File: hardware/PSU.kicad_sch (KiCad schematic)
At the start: 19 parts, among them J1 UJ20-C-H-G-SMT-2A-P16-TR, U2 REF35330QDBVR, U4 LM27762, U5 NCP1117-3.3_SOT223

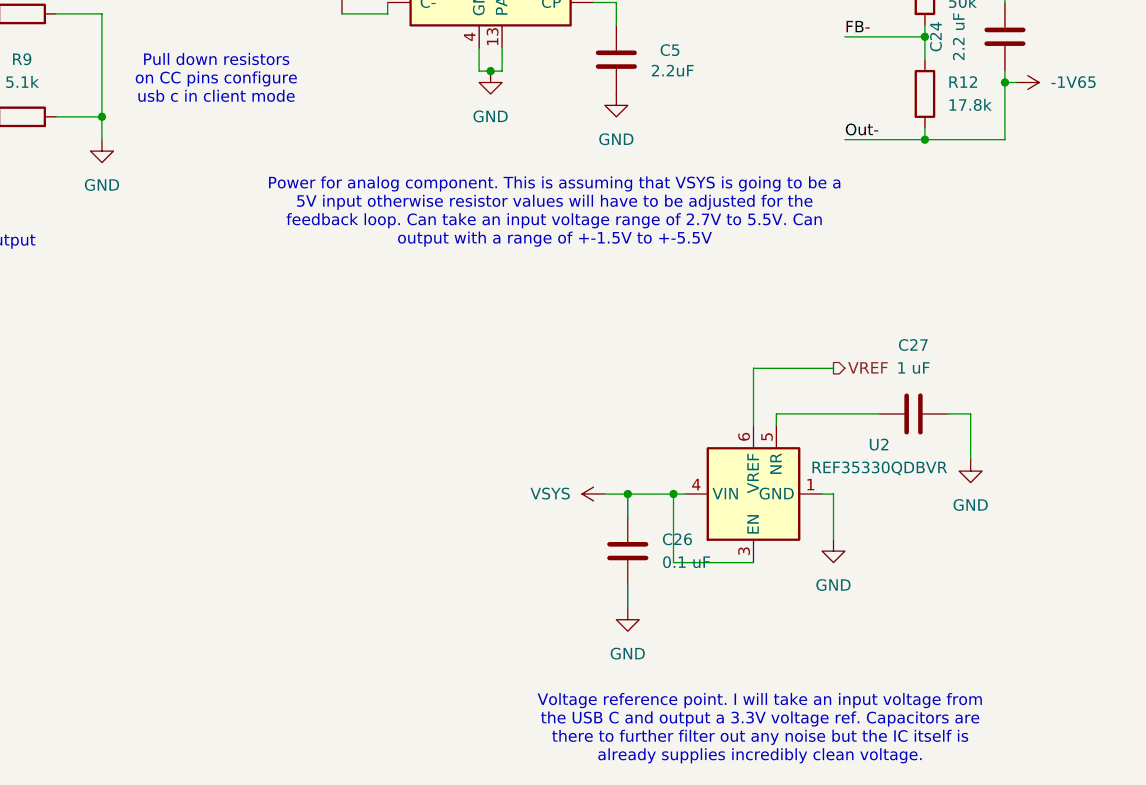
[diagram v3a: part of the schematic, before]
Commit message: "Updated PSU, Updated spreadsheets
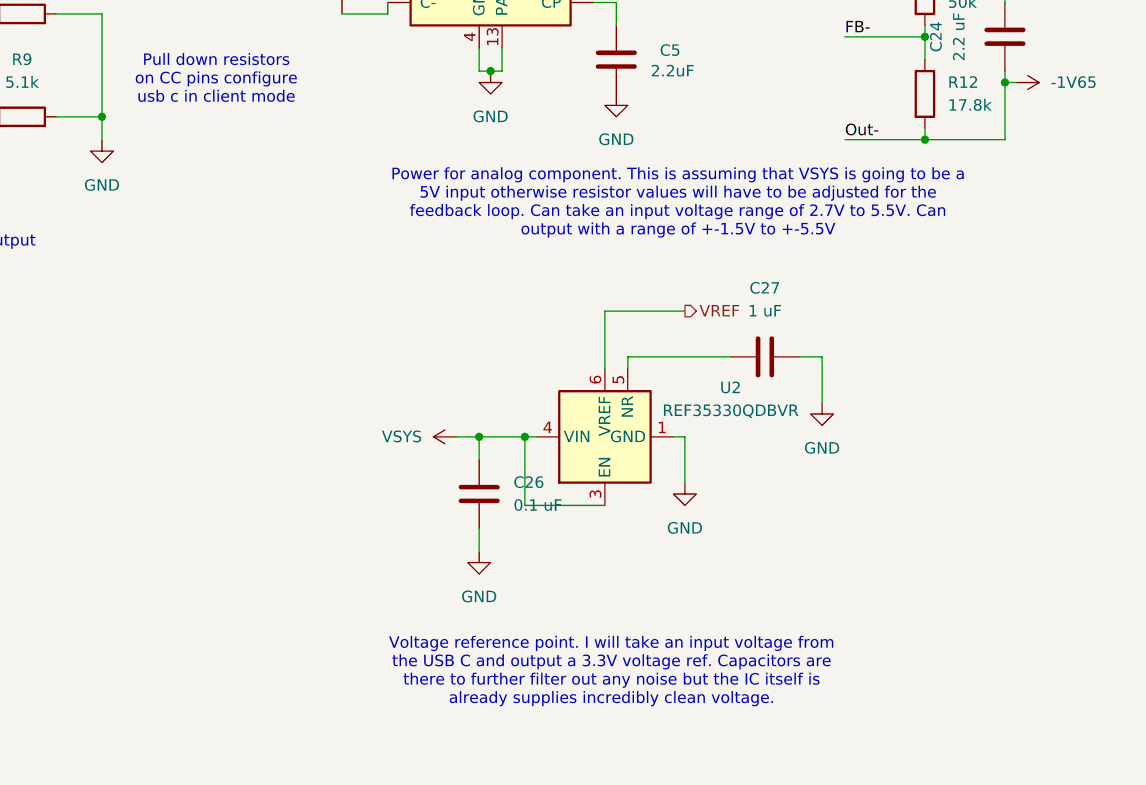
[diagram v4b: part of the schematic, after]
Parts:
- U2: Price (none) -> $2.16; Purchase Link (none) -> https://www.digikey.com/en/products/detail/texas-instrument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
- U5: Price (none) -> $0.33; Purchase Link (none) -> https://www.digikey.com/en/products/detail/onsemi/NCP1117LP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
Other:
- moved on the sheet: C26, C27, U2
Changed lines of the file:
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@@
 	(text "Power for analog component. This is assuming that VSYS is going to be a \n5V input otherwise resistor values will have to be adjusted for the \nfeedback loop. Can take an input voltage range of 2.7V to 5.5V. Can \noutput with a range of +-1.5V to +-5.5V"
 		(exclude_from_sim no)
-		(at 176.022 97.028 0)
+		(at 189.738 96.012 0)
 		(effects
 			(font
@@
 	(text "Voltage reference point. I will take an input voltage from \nthe USB C and output a 3.3V voltage ref. Capacitors are \nthere to further filter out any noise but the IC itself is \nalready supplies incredibly clean voltage."
 		(exclude_from_sim no)
-		(at 198.882 154.432 0)
+		(at 182.372 148.082 0)
 		(effects
 			(font
@@
 	)
 	(junction
-		(at 189.23 128.27)
+		(at 172.72 121.92)
 		(diameter 0)
 		(color 0 0 0 0)
@@
 	)
 	(junction
-		(at 184.15 128.27)
+		(at 167.64 121.92)
 		(diameter 0)
 		(color 0 0 0 0)
@@
 	(wire
 		(pts
-			(xy 200.66 120.65) (xy 200.66 119.38)
+			(xy 184.15 114.3) (xy 184.15 113.03)
 		)
 		(stroke
@@
 	(wire
 		(pts
-			(xy 198.12 120.65) (xy 198.12 114.3)
+			(xy 181.61 114.3) (xy 181.61 107.95)
 		)
 		(stroke
@@
 	(wire
 		(pts
-			(xy 205.74 128.27) (xy 207.01 128.27)
+			(xy 189.23 121.92) (xy 190.5 121.92)
 		)
 		(stroke
@@
 	(wire
 		(pts
-			(xy 184.15 128.27) (xy 184.15 130.81)
+			(xy 167.64 121.92) (xy 167.64 124.46)
 		)
 		(stroke
@@
 	(wire
 		(pts
-			(xy 189.23 128.27) (xy 190.5 128.27)
+			(xy 172.72 121.92) (xy 173.99 121.92)
 		)
 		(stroke
@@
 	(wire
 		(pts
-			(xy 189.23 135.89) (xy 189.23 128.27)
+			(xy 172.72 129.54) (xy 172.72 121.92)
 		)
 		(stroke
@@
 	(wire
 		(pts
-			(xy 198.12 135.89) (xy 189.23 135.89)
+			(xy 181.61 129.54) (xy 172.72 129.54)
 		)
 		(stroke
@@
 	(wire
 		(pts
-			(xy 184.15 128.27) (xy 189.23 128.27)
+			(xy 167.64 121.92) (xy 172.72 121.92)
 		)
 		(stroke
@@
 	(wire
 		(pts
-			(xy 207.01 128.27) (xy 207.01 133.35)
+			(xy 190.5 121.92) (xy 190.5 127)
 		)
 		(stroke
@@
 	(wire
 		(pts
-			(xy 219.71 119.38) (xy 222.25 119.38)
+			(xy 203.2 113.03) (xy 205.74 113.03)
 		)
 		(stroke
@@
 	(wire
 		(pts
-			(xy 184.15 138.43) (xy 184.15 140.97)
+			(xy 167.64 132.08) (xy 167.64 134.62)
 		)
 		(stroke
@@
 	(wire
 		(pts
-			(xy 222.25 119.38) (xy 222.25 124.46)
+			(xy 205.74 113.03) (xy 205.74 118.11)
 		)
 		(stroke
@@
 	(wire
 		(pts
-			(xy 198.12 114.3) (xy 207.01 114.3)
+			(xy 181.61 107.95) (xy 190.5 107.95)
 		)
 		(stroke
@@
 	(wire
 		(pts
-			(xy 200.66 119.38) (xy 212.09 119.38)
+			(xy 184.15 113.03) (xy 195.58 113.03)
 		)
 		(stroke
@@
 	(wire
 		(pts
-			(xy 181.61 128.27) (xy 184.15 128.27)
+			(xy 165.1 121.92) (xy 167.64 121.92)
 		)
 		(stroke
@@
 	(hierarchical_label "VREF"
 		(shape output)
-		(at 207.01 114.3 0)
+		(at 190.5 107.95 0)
 		(effects
 			(font
@@
 	(symbol
 		(lib_id "Reference_Voltage:REF35330QDBVR")
-		(at 198.12 128.27 90)
+		(at 181.61 121.92 90)
 		(unit 1)
 		(exclude_from_sim no)
@@
 		(fields_autoplaced yes)
 		(property "Reference" "U2"
-			(at 212.09 122.8246 90)
+			(at 195.58 116.4746 90)
 			(effects
 				(font
@@
 		)
 		(property "Value" "REF35330QDBVR"
-			(at 212.09 125.3646 90)
+			(at 195.58 119.0146 90)
 			(effects
 				(font
@@
 		)
 		(property "Footprint" "Package_TO_SOT_SMD:SOT-23-6"
-			(at 219.71 128.27 0)
+			(at 203.2 121.92 0)
 			(effects
 				(font
@@
 		)
 		(property "Datasheet" "https://www.ti.com/lit/ds/symlink/ref35.pdf"
-			(at 217.17 128.27 0)
+			(at 200.66 121.92 0)
 			(effects
 				(font
@@
 		)
 		(property "Description" "3.3V, Ultra Low-Power, High-Precision Voltage Reference, SOT-23-6"
-			(at 179.07 128.27 0)
+			(at 162.56 121.92 0)
+			(effects
+				(font
+					(size 1.27 1.27)
+				)
+				(hide yes)
+			)
+		)
+		(property "Price" "$2.16"
+			(at 181.61 121.92 90)
+			(effects
+				(font
+					(size 1.27 1.27)
+				)
+				(hide yes)
+			)
+		)
+		(property "Purchase Link" "https://www.digikey.com/en/products/detail/texas-instruments/REF35330QDBVR/18111313"
+			(at 181.61 121.92 90)
 			(effects
 				(font
@@
 	(symbol
 		(lib_id "power:GND")
-		(at 222.25 124.46 0)
+		(at 205.74 118.11 0)
 		(unit 1)
 		(exclude_from_sim no)
@@
 		(fields_autoplaced yes)
 		(property "Reference" "#PWR043"
-			(at 222.25 130.81 0)
+			(at 205.74 124.46 0)
 			(effects
 				(font
@@
 		)
 		(property "Value" "GND"
-			(at 222.25 129.54 0)
+			(at 205.74 123.19 0)
 			(effects
 				(font
@@
 		)
 		(property "Footprint" ""
-			(at 222.25 124.46 0)
+			(at 205.74 118.11 0)
 			(effects
 				(font
@@
 		)
 		(property "Datasheet" ""
-			(at 222.25 124.46 0)
+			(at 205.74 118.11 0)
 			(effects
 				(font
@@
 		)
 		(property "Description" "Power symbol creates a global label with name \"GND\" , ground"
-			(at 222.25 124.46 0)
+			(at 205.74 118.11 0)
 			(effects
 				(font
@@
 	(symbol
 		(lib_id "power:GND")
-		(at 207.01 133.35 0)
+		(at 190.5 127 0)
 		(unit 1)
 		(exclude_from_sim no)
@@
 		(fields_autoplaced yes)
 		(property "Reference" "#PWR042"
-			(at 207.01 139.7 0)
+			(at 190.5 133.35 0)
 			(effects
 				(font
@@
 		)
 		(property "Value" "GND"
-			(at 207.01 138.43 0)
+			(at 190.5 132.08 0)
 			(effects
 				(font
@@
 		)
 		(property "Footprint" ""
-			(at 207.01 133.35 0)
+			(at 190.5 127 0)
 			(effects
 				(font
@@
 		)
 		(property "Datasheet" ""
-			(at 207.01 133.35 0)
+			(at 190.5 127 0)
 			(effects
 				(font
@@
 		)
 		(property "Description" "Power symbol creates a global label with name \"GND\" , ground"
-			(at 207.01 133.35 0)
+			(at 190.5 127 0)
 			(effects
 				(font
@@
 	(symbol
 		(lib_id "Device:C")
-		(at 215.9 119.38 270)
+		(at 199.39 113.03 270)
 		(unit 1)
 		(exclude_from_sim no)
@@
 		(fields_autoplaced yes)
 		(property "Reference" "C27"
-			(at 215.9 111.76 90)
+			(at 199.39 105.41 90)
 			(effects
 				(font
@@
 		)
 		(property "Value" "1 uF"
-			(at 215.9 114.3 90)
+			(at 199.39 107.95 90)
 			(effects
 				(font
@@
 		)
 		(property "Footprint" ""
-			(at 212.09 120.3452 0)
+			(at 195.58 113.9952 0)
 			(effects
 				(font
@@
 		)
 		(property "Datasheet" "~"
-			(at 215.9 119.38 0)
+			(at 199.39 113.03 0)
 			(effects
 				(font
@@
 		)
 		(property "Description" "Unpolarized capacitor"
-			(at 215.9 119.38 0)
+			(at 199.39 113.03 0)
 			(effects
 				(font
@@
 	(symbol
 		(lib_id "Device:C")
-		(at 184.15 134.62 0)
+		(at 167.64 128.27 0)
 		(unit 1)
 		(exclude_from_sim no)
@@
 		(fields_autoplaced yes)
 		(property "Reference" "C26"
-			(at 187.96 133.3499 0)
+			(at 171.45 126.9999 0)
 			(effects
 				(font
@@
 		)
 		(property "Value" "0.1 uF"
-			(at 187.96 135.8899 0)
+			(at 171.45 129.5399 0)
 			(effects
 				(font
@@
 		)
 		(property "Footprint" ""
-			(at 185.1152 138.43 0)
+			(at 168.6052 132.08 0)
 			(effects
 				(font
@@
 		)
 		(property "Datasheet" "~"
-			(at 184.15 134.62 0)
+			(at 167.64 128.27 0)
 			(effects
 				(font
@@
 		)
 		(property "Description" "Unpolarized capacitor"
-			(at 184.15 134.62 0)
+			(at 167.64 128.27 0)
 			(effects
 				(font
@@
 			)
 		)
+		(property "Purchase Link" "https://www.digikey.com/en/products/detail/onsemi/NCP1117LPST33T3G/2194024"
+			(at 85.09 113.03 0)
+			(effects
+				(font
+					(size 1.27 1.27)
+				)
+				(hide yes)
+			)
+		)
+		(property "Price" "$0.33"
+			(at 85.09 113.03 0)
+			(effects
+				(font
+					(size 1.27 1.27)
+				)
+				(hide yes)
+			)
+		)
 		(pin "2"
 		)
@@
 	(symbol
 		(lib_id "power:VDC")
-		(at 181.61 128.27 90)
+		(at 165.1 121.92 90)
 		(unit 1)
 		(exclude_from_sim no)
@@
 		(fields_autoplaced yes)
 		(property "Reference" "#PWR040"
-			(at 185.42 128.27 0)
+			(at 168.91 121.92 0)
 			(effects
 				(font
@@
 		)
 		(property "Value" "VSYS"
-			(at 177.8 128.2699 90)
+			(at 161.29 121.9199 90)
 			(effects
 				(font
@@
 		)
 		(property "Footprint" ""
-			(at 181.61 128.27 0)
+			(at 165.1 121.92 0)
 			(effects
 				(font
@@
 		)
 		(property "Datasheet" ""
-			(at 181.61 128.27 0)
+			(at 165.1 121.92 0)
 			(effects
 				(font
@@
 		)
 		(property "Description" "Power symbol creates a global label with name \"VDC\""
-			(at 181.61 128.27 0)
+			(at 165.1 121.92 0)
 			(effects
 				(font
@@
 	(symbol
 		(lib_id "power:GND")
-		(at 184.15 140.97 0)
+		(at 167.64 134.62 0)
 		(unit 1)
 		(exclude_from_sim no)
@@
 		(fields_autoplaced yes)
 		(property "Reference" "#PWR041"
-			(at 184.15 147.32 0)
+			(at 167.64 140.97 0)
 			(effects
 				(font
@@
 		)
 		(property "Value" "GND"
-			(at 184.15 146.05 0)
+			(at 167.64 139.7 0)
 			(effects
 				(font
@@
 		)
 		(property "Footprint" ""
-			(at 184.15 140.97 0)
+			(at 167.64 134.62 0)
 			(effects
 				(font
@@
 		)
 		(property "Datasheet" ""
-			(at 184.15 140.97 0)
+			(at 167.64 134.62 0)
 			(effects
 				(font
@@
 		)
 		(property "Description" "Power symbol creates a global label with name \"GND\" , ground"
-			(at 184.15 140.97 0)
+			(at 167.64 134.62 0)
 			(effects
 				(font

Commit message: Up to date
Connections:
- net +3V3 is gone; now on net VSYS: C21.1, U5.2 (VO)
- net VSYS: no longer C1.1, C25.1, J1.A4_B9 (VBUS), J1.B4_A9 (VBUS), U4.12 (EN+), U4.3 (VIN), U4.8 (EN-), U5.3 (VI)
- net +1V65 renamed 1V65
- new net VBUS: C1.1, C25.1, J1.A4_B9 (VBUS), J1.B4_A9 (VBUS), U4.12 (EN+), U4.3 (VIN), U4.8 (EN-), U5.3 (VI)
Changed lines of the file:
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@@
+		)
+	)
+	(hierarchical_label "-1V65"
+		(shape output)
+		(at 227.33 82.55 0)
+		(effects
+			(font
+				(size 1.27 1.27)
+			)
+			(justify left)
+		)
+	)
+	(hierarchical_label "VSYS"
+		(shape output)
+		(at 111.76 110.49 0)
+		(effects
+			(font
+				(size 1.27 1.27)
+			)
+			(justify left)
+		)
+	)
+	(hierarchical_label "1V65"
+		(shape output)
+		(at 227.33 48.26 0)
+		(effects
+			(font
+				(size 1.27 1.27)
+			)
+			(justify left)
 		)
 	)
@@
 	)
 	(symbol
-		(lib_id "power:VDC")
-		(at 227.33 48.26 270)
-		(unit 1)
-		(exclude_from_sim no)
-		(in_bom yes)
-		(on_board yes)
-		(dnp no)
-		(fields_autoplaced yes)
-		(property "Reference" "#PWR030"
-			(at 223.52 48.26 0)
-			(effects
-				(font
-					(size 1.27 1.27)
-				)
-				(hide yes)
-			)
-		)
-		(property "Value" "+1V65"
-			(at 231.14 48.2599 90)
-			(effects
-				(font
-					(size 1.27 1.27)
-				)
-				(justify left)
-			)
-		)
-		(property "Footprint" ""
-			(at 227.33 48.26 0)
-			(effects
-				(font
-					(size 1.27 1.27)
-				)
-				(hide yes)
-			)
-		)
-		(property "Datasheet" ""
-			(at 227.33 48.26 0)
-			(effects
-				(font
-					(size 1.27 1.27)
-				)
-				(hide yes)
-			)
-		)
-		(property "Description" "Power symbol creates a global label with name \"VDC\""
-			(at 227.33 48.26 0)
-			(effects
-				(font
-					(size 1.27 1.27)
-				)
-				(hide yes)
-			)
-		)
-		(pin "1"
-		)
-		(instances
-			(project ""
-				(path "/94683f5c-9cd9-448e-be96-9792537b5cb8/6296dfbc-bf5e-4649-b078-009c1ac21de6"
-					(reference "#PWR030")
-					(unit 1)
-				)
-			)
-		)
-	)
-	(symbol
 		(lib_name "GND_3")
 		(lib_id "power:GND")
@@
 	)
 	(symbol
-		(lib_id "power:+3V3")
-		(at 111.76 110.49 0)
-		(unit 1)
-		(exclude_from_sim no)
-		(in_bom yes)
-		(on_board yes)
-		(dnp no)
-		(fields_autoplaced yes)
-		(property "Reference" "#PWR011"
-			(at 111.76 114.3 0)
-			(effects
-				(font
-					(size 1.27 1.27)
-				)
-				(hide yes)
-			)
-		)
-		(property "Value" "+3V3"
-			(at 111.76 105.41 0)
-			(effects
-				(font
-					(size 1.27 1.27)
-				)
-			)
-		)
-		(property "Footprint" ""
-			(at 111.76 110.49 0)
-			(effects
-				(font
-					(size 1.27 1.27)
-				)
-				(hide yes)
-			)
-		)
-		(property "Datasheet" ""
-			(at 111.76 110.49 0)
-			(effects
-				(font
-					(size 1.27 1.27)
-				)
-				(hide yes)
-			)
-		)
-		(property "Description" "Power symbol creates a global label with name \"+3V3\""
-			(at 111.76 110.49 0)
-			(effects
-				(font
-					(size 1.27 1.27)
-				)
-				(hide yes)
-			)
-		)
-		(pin "1"
-		)
-		(instances
-			(project ""
-				(path "/94683f5c-9cd9-448e-be96-9792537b5cb8/6296dfbc-bf5e-4649-b078-009c1ac21de6"
-					(reference "#PWR011")
-					(unit 1)
-				)
-			)
-		)
-	)
-	(symbol
 		(lib_id "Device:R")
 		(at 116.84 74.93 90)
@@
 			)
 		)
-		(property "Value" "VSYS"
-			(at 59.69 105.41 0)
-			(effects
-				(font
-					(size 1.27 1.27)
-				)
+		(property "Value" "VBUS"
+			(at 62.23 109.2199 0)
+			(effects
+				(font
+					(size 1.27 1.27)
+				)
+				(justify left)
 			)
 		)
@@
 			)
 		)
-		(property "Value" "VSYS"
-			(at 91.44 41.91 0)
-			(effects
-				(font
-					(size 1.27 1.27)
-				)
+		(property "Value" "VBUS"
+			(at 93.98 45.7199 0)
+			(effects
+				(font
+					(size 1.27 1.27)
+				)
+				(justify left)
 			)
 		)
@@
 		(on_board yes)
 		(dnp no)
-		(fields_autoplaced yes)
 		(property "Reference" "#PWR037"
 			(at 140.97 57.15 0)
@@
 			)
 		)
-		(property "Value" "VSYS"
+		(property "Value" "VBUS"
 			(at 140.97 48.26 0)
 			(effects
@@
 					(unit 1)
 				)
-			)
-		)
-	)
-	(symbol
-		(lib_id "power:VDC")
-		(at 227.33 82.55 270)
-		(unit 1)
-		(exclude_from_sim no)
-		(in_bom yes)
-		(on_board yes)
-		(dnp no)
-		(property "Reference" "#PWR039"
-			(at 223.52 82.55 0)
-			(effects
-				(font
-					(size 1.27 1.27)
-				)
-				(hide yes)
-			)
-		)
-		(property "Value" "-1V65"
-			(at 231.14 82.55 90)
-			(effects
-				(font
-					(size 1.27 1.27)
-				)
-				(justify left)
-			)
-		)
-		(property "Footprint" ""
-			(at 227.33 82.55 0)
-			(effects
-				(font
-					(size 1.27 1.27)
-				)
-				(hide yes)
-			)
-		)
-		(property "Datasheet" ""
-			(at 227.33 82.55 0)
-			(effects
-				(font
-					(size 1.27 1.27)
-				)
-				(hide yes)
-			)
-		)
-		(property "Description" "Power symbol creates a global label with name \"VDC\""
-			(at 227.33 82.55 0)
-			(effects
-				(font
-					(size 1.27 1.27)
-				)
-				(hide yes)
-			)
-		)
-		(pin "1"
-		)
-		(instances
-			(project ""
-				(path "/94683f5c-9cd9-448e-be96-9792537b5cb8/6296dfbc-bf5e-4649-b078-009c1ac21de6"
-					(reference "#PWR039")
-					(unit 1)
-				)
